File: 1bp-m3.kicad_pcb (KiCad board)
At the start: 2 copper layers, 27.5 x 24.8 mm, 33 parts, among them J1 TCS7913-43, P13 TP_50, P7 TP_50, P8 TP_50, P9 TP_50, U1 TL972IDR

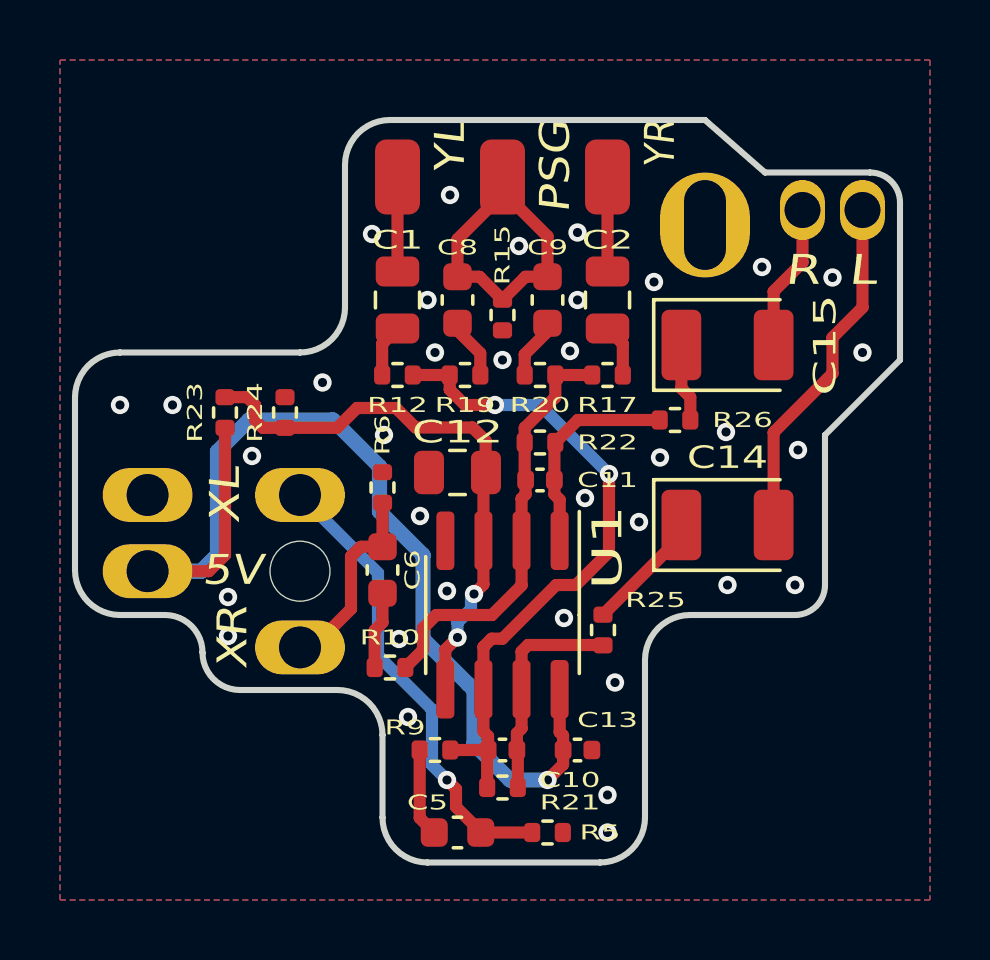
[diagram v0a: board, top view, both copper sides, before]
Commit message: updated silkscreen for OSHW
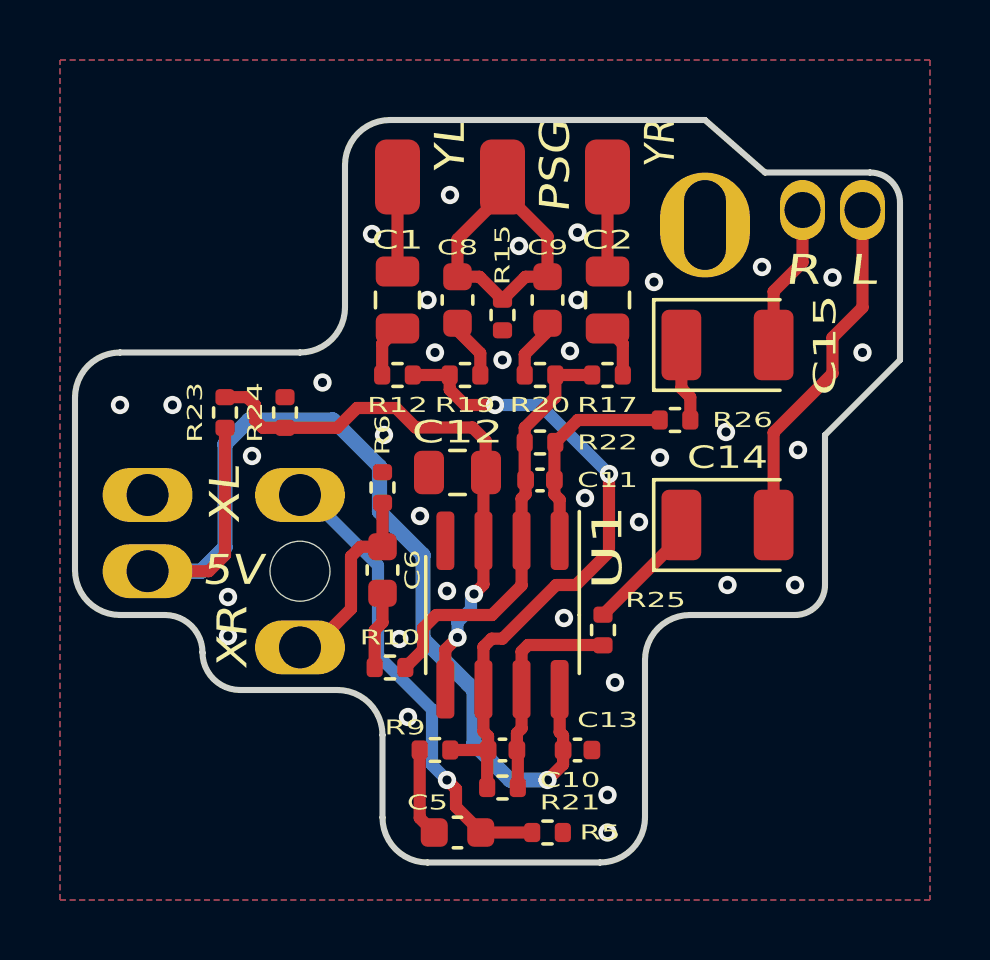
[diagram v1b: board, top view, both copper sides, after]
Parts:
- added LOGO1: Logo_Open_Hardware_Small, Symbol:OSHW-Logo2_7.3x6mm_SilkScreen, B.Cu at (130.2, 98.5)
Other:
- board text added: "GENESIS 3"
- board text added: "STEREO MOD"
- board text added: "https://github.com/ LateToTheGame16/ Genesis-Model3-Stereo"
- board text removed: "GENESIS 3 AUDIO BYPASS"

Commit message: export gerbers
first fab run
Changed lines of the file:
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@@
     (solder_mask_min_width 0.25)
     (pcbplotparams
-      (layerselection 0x00012fc_ffffffff)
+      (layerselection 0x00010f8_ffffffff)
       (disableapertmacros false)
       (usegerberextensions false)
-      (usegerberattributes false)
+      (usegerberattributes true)
       (usegerberadvancedattributes false)
       (creategerberjobfile true)
       (svguseinch false)
       (svgprecision 6)
-      (excludeedgelayer false)
-      (plotframeref true)
+      (excludeedgelayer true)
+      (plotframeref false)
       (viasonmask false)
       (mode 1)
@@
   )
   (footprint "Resistor_SMD:R_0402_1005Metric" (layer "F.Cu")
-    (at 129.750007 84.500009 -90)
+    (at 129.75 84.5 -90)
     (descr "Resistor SMD 0402 (1005 Metric), square (rectangular) end terminal, IPC_7351 nominal, (Body size source: IPC-SM-782 page 72, https://www.pcb-3d.com/wordpress/wp-content/uploads/ipc-sm-782a_amendment_1_and_2.pdf), generated with kicad-footprint-generator")
     (tags "resistor")
@@
   )
   (footprint "Resistor_SMD:R_0402_1005Metric" (layer "F.Cu")
-    (at 125.74999 90.25001 90)
+    (at 125.75 90.25 90)
     (descr "Resistor SMD 0402 (1005 Metric), square (rectangular) end terminal, IPC_7351 nominal, (Body size source: IPC-SM-782 page 72, https://www.pcb-3d.com/wordpress/wp-content/uploads/ipc-sm-782a_amendment_1_and_2.pdf), generated with kicad-footprint-generator")
     (tags "resistor")
@@
   )
   (footprint "Capacitor_SMD:C_0603_1608Metric" (layer "F.Cu")
-    (at 128.25001 84.00001 -90)
+    (at 128.25 84 -90)
     (descr "Capacitor SMD 0603 (1608 Metric), square (rectangular) end terminal, IPC_7351 nominal, (Body size source: IPC-SM-782 page 76, https://www.pcb-3d.com/wordpress/wp-content/uploads/ipc-sm-782a_amendment_1_and_2.pdf), generated with kicad-footprint-generator")
     (tags "capacitor")
@@
   )
   (footprint "Capacitor_SMD:C_0402_1005Metric" (layer "F.Cu")
-    (at 132.250002 99.000005)
+    (at 132.25 99)
     (descr "Capacitor SMD 0402 (1005 Metric), square (rectangular) end terminal, IPC_7351 nominal, (Body size source: IPC-SM-782 page 76, https://www.pcb-3d.com/wordpress/wp-content/uploads/ipc-sm-782a_amendment_1_and_2.pdf), generated with kicad-footprint-generator")
     (tags "capacitor")
@@
   )
   (footprint "Package_SO:SOIC-8_3.9x4.9mm_P1.27mm" (layer "F.Cu")
-    (at 129.750007 94.499989 -90)
+    (at 129.75 94.5 -90)
     (descr "SOIC, 8 Pin (JEDEC MS-012AA, https://www.analog.com/media/en/package-pcb-resources/package/pkg_pdf/soic_narrow-r/r_8.pdf), generated with kicad-footprint-generator ipc_gullwing_generator.py")
     (tags "SOIC SO")
@@
   )
   (footprint "Capacitor_SMD:C_0805_2012Metric" (layer "F.Cu")
-    (at 128.25001 89.750011)
+    (at 128.25 89.75)
     (descr "Capacitor SMD 0805 (2012 Metric), square (rectangular) end terminal, IPC_7351 nominal, (Body size source: IPC-SM-782 page 76, https://www.pcb-3d.com/wordpress/wp-content/uploads/ipc-sm-782a_amendment_1_and_2.pdf, https://docs.google.com/spreadsheets/d/1BsfQQcO9C6DZCsRaXUlFlo91Tg2WpOkGARC1WS5S8t0/edit?usp=sharing), generated with kicad-footprint-generator")
     (tags "capacitor")
@@
   )
   (footprint "Capacitor_Tantalum_SMD:CP_EIA-3528-21_Kemet-B" (layer "F.Cu")
-    (at 137.249992 85.500007)
+    (at 137.25 85.5)
     (descr "Tantalum Capacitor SMD Kemet-B (3528-21 Metric), IPC_7351 nominal, (Body size from: http://www.kemet.com/Lists/ProductCatalog/Attachments/253/KEM_TC101_STD.pdf), generated with kicad-footprint-generator")
     (tags "capacitor tantalum")
@@
   (segment (start 127.4 97.65) (end 125.6 95.85) (width 0.4064) (layer "B.Cu") (net 6))
   (segment (start 127.4 99.5) (end 127.4 97.65) (width 0.4064) (layer "B.Cu") (net 6))
-  (segment (start 123.25 90.5) (end 123 90.5) (width 0.4064) (layer "B.Cu") (net 6))
   (segment (start 125.6 92.85) (end 123.25 90.5) (width 0.4064) (layer "B.Cu") (net 6))
   (segment (start 125.6 95.85) (end 125.6 92.85) (width 0.4064) (layer "B.Cu") (net 6))
@@
   (segment (start 129.01 86.5) (end 129.01 85.7725) (width 0.4064) (layer "F.Cu") (net 17))
   (segment (start 129.01 85.7725) (end 128.25001 85.01251) (width 0.4064) (layer "F.Cu") (net 17))
-  (segment (start 128.25001 85.01251) (end 128.25001 84.77501) (width 0.4064) (layer "F.Cu") (net 17))
   (segment (start 131.25 83.225) (end 130.515 83.225) (width 0.4064) (layer "F.Cu") (net 18))
   (segment (start 128.25 83.225) (end 128.25 81.975) (width 0.4064) (layer "F.Cu") (net 18))
